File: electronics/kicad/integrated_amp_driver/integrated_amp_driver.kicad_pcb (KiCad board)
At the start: 2 copper layers, 39 parts, among them J2 PDSE1, J3 Conn_01x04, P1 CONN_6, P2 CONN_6, P4 CONN_6, P5 CONN_6, U1 LM7805, U14 MCP4725SOT-23, U15 TS912IDT, U16 MCP4725SOT-23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

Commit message: Driver
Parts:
- removed P1: CONN_6, Connectors2:1X06-SMD_RA_MALE
- removed U2: Teensy-LC, teensy:Teensy30_31_32_LC
- added C10: 0.1 uF, Capacitors:0603, F.Cu at (160.8, 88.5)
- added C11: 0.1 uF, Capacitors:0603, F.Cu at (175.9, 107.6)
- added C4: 10uF, Capacitors:1206, F.Cu at (160.3, 93.6)
- added C5: 0.1 uF, Capacitors:0603, F.Cu at (160.3, 100.2)
- added C6: 0.1 uF, Capacitors:0603, F.Cu at (169.0, 112.5)
- added C8: 0.1 uF, Capacitors:0603, F.Cu at (172.2, 113.4)
- added C9: 0.1 uF, Capacitors:0603, F.Cu at (182.4, 105.8)
- added J1: Conn_01x14_Female, Connector_PinHeader_2.54mm:PinHeader_1x14_P2.54mm_Vertical_SMD_Pin1Right, F.Cu at (107.2, 150.4)
- added J4: Conn_01x14_Female, Connector_PinHeader_2.54mm:PinHeader_1x14_P2.54mm_Vertical_SMD_Pin1Right, F.Cu at (122.4, 150.4)
- added J5: CONN_03, Connectors2:1X03_SMD_RA_MALE, F.Cu at (182.8, 89.6)
- added JP1: Jumper, 0xDBFB7:JUMPER_5104, F.Cu at (130.7, 107.6)
- moved J3 72.6 mm to (89.3, 152.3)
- moved J2 48.2 mm to (170.4, 91.1), turned to 90 degrees
- moved U3 47.6 mm to (167.0, 100.3)
- moved R15 42.8 mm to (131.4, 139.6)
- moved R11 39.3 mm to (155.7, 130.9)
- moved U4 38.3 mm to (193.4, 94.0)
- moved R6 37.8 mm to (130.3, 132.3), turned to 90 degrees
- moved U16 35.2 mm to (153.2, 133.5), turned to 90 degrees
- moved C7 32.7 mm to (172.0, 133.0), turned to 180 degrees
- moved C3 32.7 mm to (167.0, 121.4)
- moved C12 30.9 mm to (174.6, 129.5), turned to 90 degrees
- moved R13 27.5 mm to (158.0, 131.7), turned to 270 degrees
- moved P2 25.9 mm to (88.6, 129.8)
- moved P4 25.5 mm to (174.6, 116.3)
- moved P5 25.5 mm to (174.6, 131.6)
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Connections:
- P2 pad 1: Net-(P2-Pad1) -> RX0
- P2 pad 2: Net-(P2-Pad2) -> TX0
- P2 pad 3: Net-(P2-Pad3) -> GND
- P2 pad 4: Net-(P2-Pad4) -> RX3
- P2 pad 5: Net-(P2-Pad5) -> TX3
- P2 pad 6: Net-(P2-Pad6) -> GND
- U4 pad 1: Net-(U4-Pad1) -> GND
- U4 pad 2: Net-(U4-Pad2) -> 3.3V
- U4 pad 3: Net-(U4-Pad3) -> 12V
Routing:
- net 5V: track 0.00 -> 137.1 mm
- net 3.3V: track 0.00 -> 53.3 mm, vias 0 -> 1
- net GND: track 0.00 -> 25.3 mm
- net AMP_GATE_CONTROL_: track 0.00 -> 23.7 mm
- net AMP_GAIN_CONTROL_: track 0.00 -> 16.6 mm
- net 12V: track 0.00 -> 11.4 mm
- net Vtune: track 0.00 -> 10.5 mm
- net 20V: track 0.00 -> 7.52 mm
- net Net-(R10-Pad2): track 0.00 -> 7.42 mm
- net -5V: track 0.00 -> 6.29 mm
- net Net-(R1-Pad2): track 0.00 -> 4.78 mm
- net AMP_DRAIN_SUPPLY: track 0.00 -> 4.65 mm
- net Net-(U6-Pad1): track 0.00 -> 4.59 mm
- net 24V: track 0.00 -> 4.23 mm
- net Net-(R11-Pad2): track 0.00 -> 3.39 mm
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- added copper zone on F.Cu, net 24V
- added copper zone on F.Cu, net GND

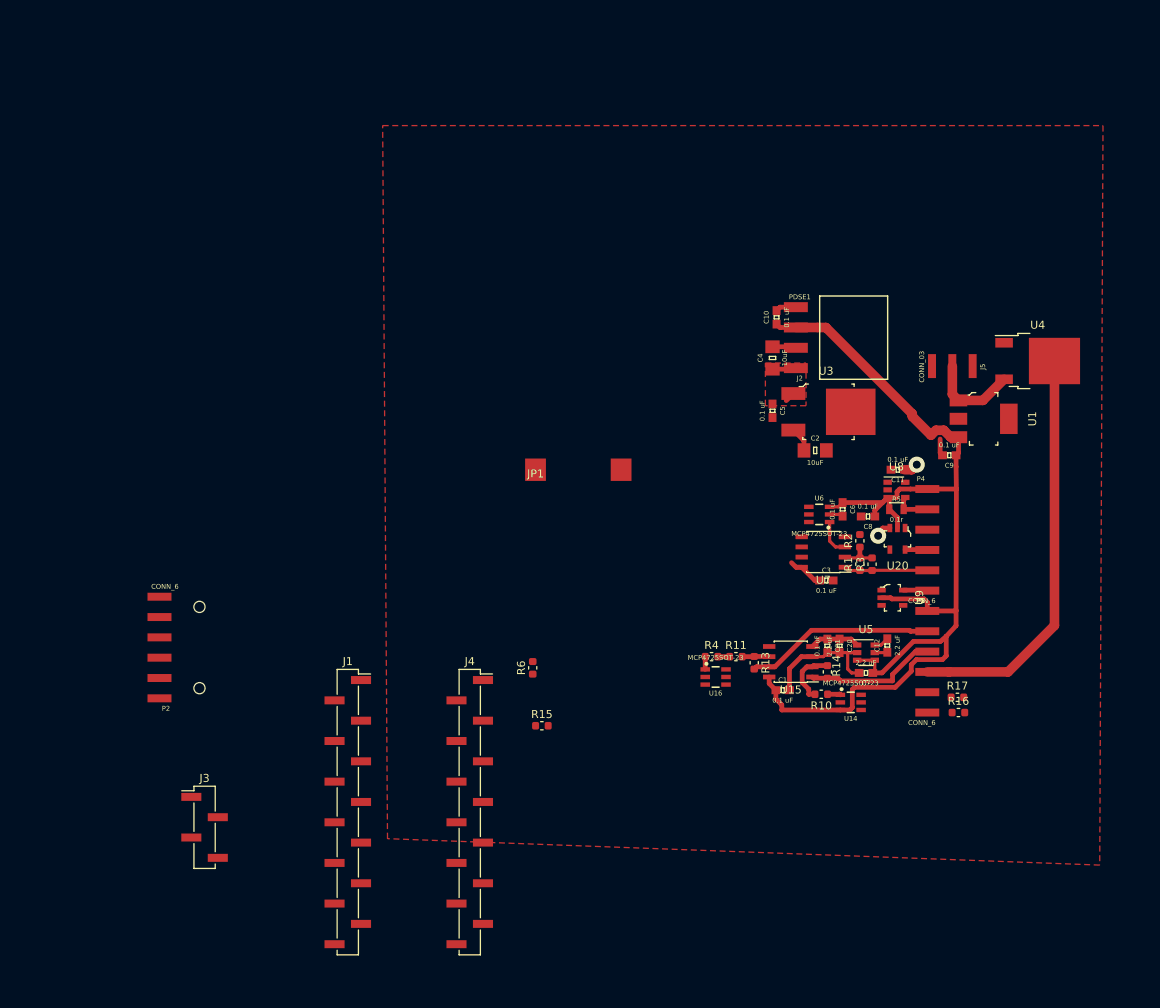
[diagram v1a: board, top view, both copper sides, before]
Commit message: Too many vias
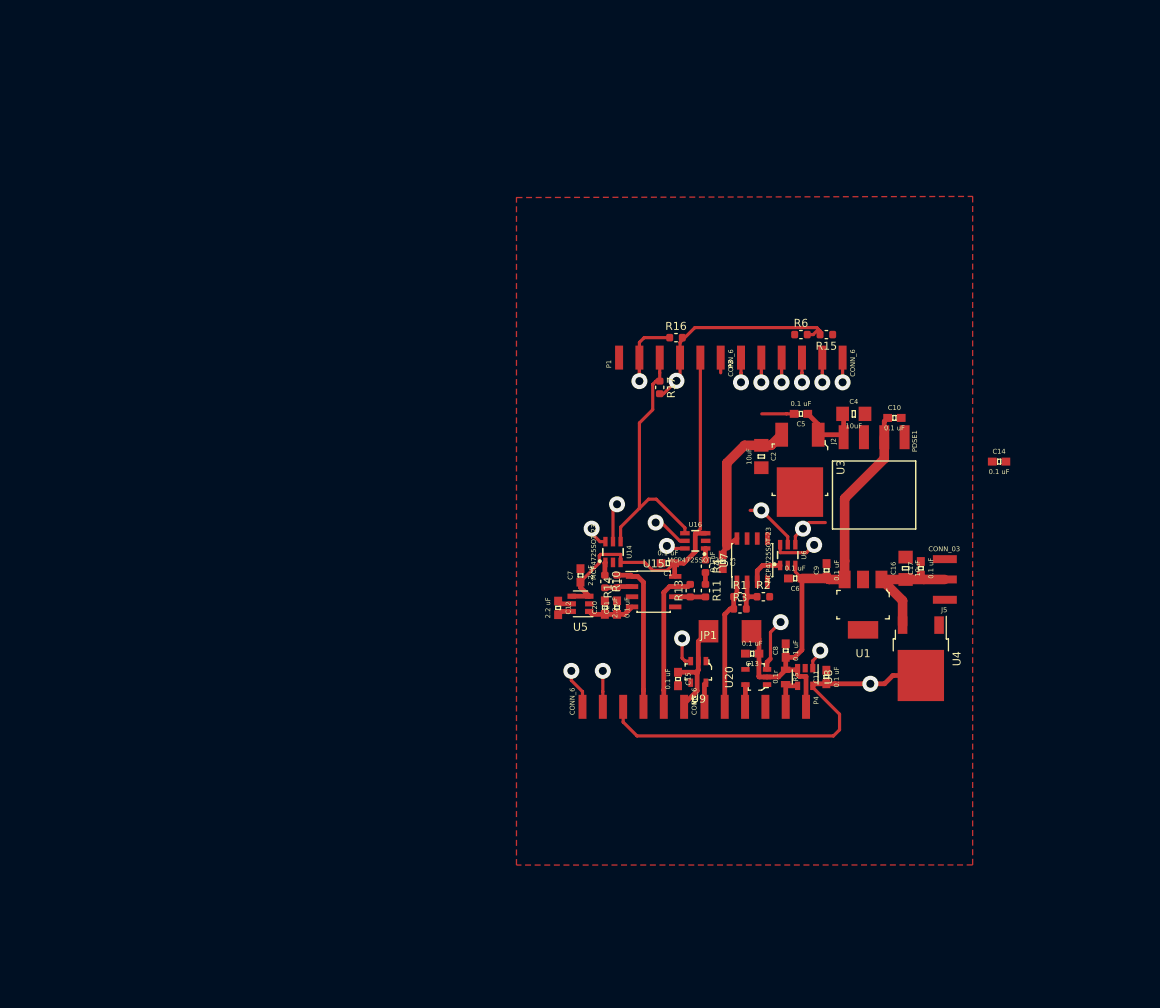
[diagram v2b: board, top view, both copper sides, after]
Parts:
- removed J1, J4: Conn_01x14_Female, Connector_PinHeader_2.54mm:PinHeader_1x14_P2.54mm_Vertical_SMD_Pin1Right
- removed J3: Conn_01x04, Connector_PinHeader_2.54mm:PinHeader_1x04_P2.54mm_Vertical_SMD_Pin1Left
- removed P2: CONN_6, Connectors2:1X06-SMD_RA_MALE
- added C13: 0.1 uF, Capacitors:0603, F.Cu at (157.7, 130.6)
- added C14: 0.1 uF, Capacitors:0603, F.Cu at (188.6, 106.6)
- added C15: 0.1 uF, Capacitors:0603, F.Cu at (148.5, 133.7)
- added C16: 10uF, Capacitors:1206, F.Cu at (176.9, 119.9)
- added C17: 0.1 uF, Capacitors:0603, F.Cu at (178.8, 119.9)
- added P1: CONN_6, Connectors2:1X06-SMD_RA_MALE, F.Cu at (147.4, 98.6)
- added P3: CONN_6, Connectors2:1X06-SMD_RA_MALE, F.Cu at (162.7, 98.6)
- JP1: footprint 0xDBFB7:JUMPER_5104 -> 0xDBFB7:JUMPER_5102
- moved R15 60.5 mm to (167.0, 90.7), turned to 180 degrees
- moved R16 58.7 mm to (148.2, 91.1)
- moved R17 53.7 mm to (146.2, 97.3), turned to 270 degrees
- moved R6 53.5 mm to (163.8, 90.7), turned to 0 degrees
- moved C12 41.4 mm to (133.5, 124.8), turned to 270 degrees
- moved U4 40.0 mm to (178.8, 131.2), turned to 270 degrees
- moved C7 37.7 mm to (136.3, 120.8), turned to 90 degrees
- moved U5 36.2 mm to (136.3, 124.3), turned to 180 degrees
- moved U14 35.2 mm to (140.3, 117.9), turned to 180 degrees
- moved J5 31.9 mm to (186.8, 121.3), turned to 90 degrees
- moved P5 31.8 mm to (142.9, 132.2), turned to 180 degrees
- moved R10 30.5 mm to (139.3, 121.5), turned to 270 degrees
- moved C20 29.7 mm to (139.3, 124.8), turned to 90 degrees
- moved JP1 29.6 mm to (152.3, 127.8)
- moved R14 28.6 mm to (140.8, 121.5), turned to 90 degrees
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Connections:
- J5 pad 3: Net-(J5-Pad3) -> GND
- JP1 pad 1: Net-(JP1-Pad1) -> 5V
- JP1 pad 2: Net-(JP1-Pad2) -> 5V
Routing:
- net SDA: track 0.00 -> 43.6 mm, vias 0 -> 2
- net SCL: track 0.00 -> 32.4 mm, vias 0 -> 5
- net 3.3V: track 53.3 -> 79.2 mm, vias 1 -> 2
- net GND: track 25.3 -> 5.95 mm
- net 20V: track 7.52 -> 21.5 mm
- net 5V: track 137.1 -> 123.7 mm
- net TUNING_DAC_I2C_SELECT: track 0.00 -> 8.75 mm, vias 0 -> 2
- net ~AMP_DRAIN_CONTROL: track 2.10 -> 9.71 mm, vias 1 -> 2
- net ~VCO_POWER_CONTROL: track 0.00 -> 6.79 mm, vias 0 -> 2
- net Vtune: track 10.5 -> 16.5 mm
- net GAIN_DAC_I2C_SELECT: track 0.00 -> 5.82 mm, vias 0 -> 2
- net current_sense_output: track 0.00 -> 5.68 mm, vias 0 -> 2
- net AMP_GATE_CONTROL_: track 23.7 -> 18.0 mm
- net GATE_DAC_I2C_SELECT: track 0.00 -> 5.48 mm, vias 0 -> 2
- net 24V: track 4.23 -> 9.43 mm
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- removed copper zone on F.Cu, net 24V

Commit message: this driver is being a right bastard
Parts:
- removed C14: 0.1 uF, Capacitors:0603
- moved R15 8.07 mm to (166.2, 98.7)
- moved R6 8.03 mm to (163.8, 98.7)
- moved R16 5.20 mm to (147.5, 96.2), turned to 270 degrees
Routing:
- net 3.3V: track 79.2 -> 84.6 mm
- net SDA: track 43.6 -> 40.5 mm
- net SCL: track 32.4 -> 35.4 mm
- net ~VCO_POWER_CONTROL: track 6.79 -> 9.25 mm
- net ~AMP_DRAIN_CONTROL: track 9.71 -> 12.0 mm
